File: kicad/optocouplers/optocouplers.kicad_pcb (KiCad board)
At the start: 2 copper layers, 18 parts, among them Q1 PN2222A, U1 ITR9608, U2 ITR9608, U3 ITR9608, U4 ITR9608, U5 ITR9608, U6 ITR9608, U7 ITR9608, U8 ITR9608

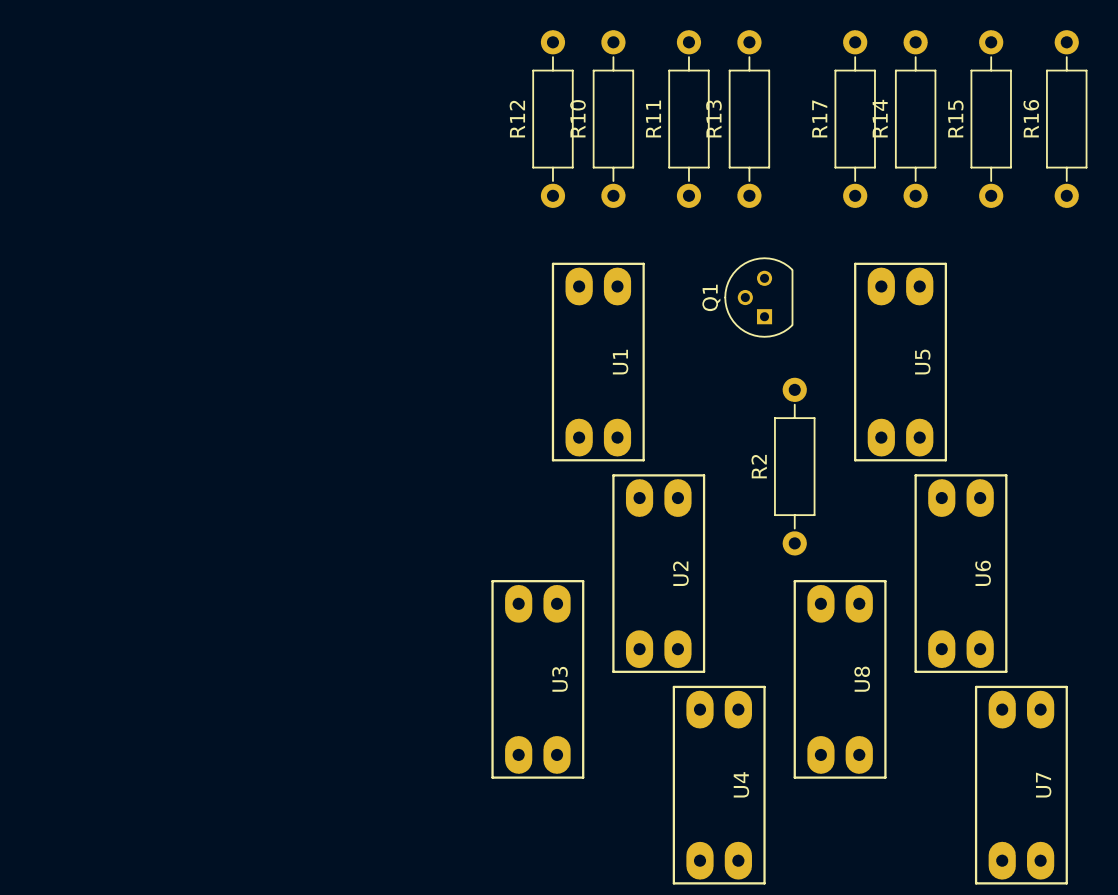
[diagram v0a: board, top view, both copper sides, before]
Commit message: update kicad drawings for optocouplers
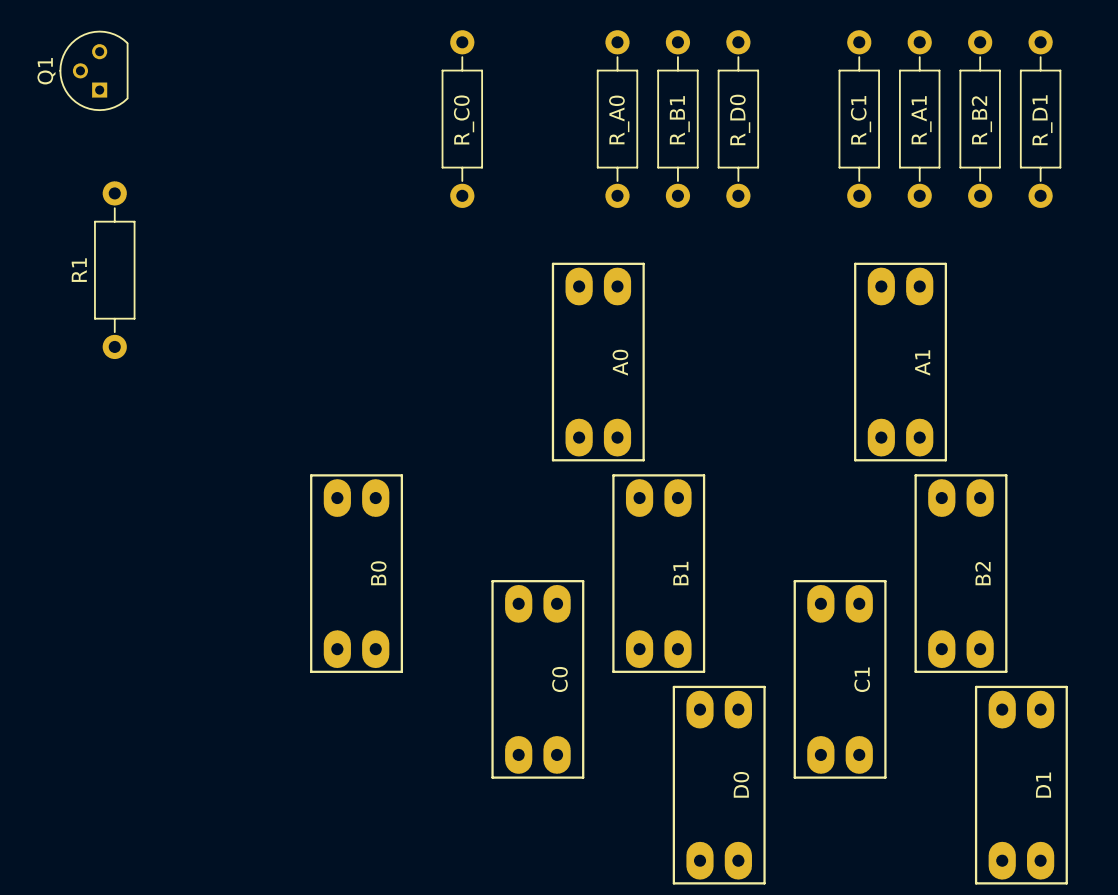
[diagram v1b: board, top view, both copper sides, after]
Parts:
- removed R10, R11, R13, R14, R15, R16, R17: 270R, Resistors_ThroughHole:R_Axial_DIN0207_L6.3mm_D2.5mm_P10.16mm_Horizontal
- added B0: ITR9608, ITR9608:ITR9608, F.Cu at (84.0, 114.0)
- added R_A0: 270R, Resistors_ThroughHole:R_Axial_DIN0207_L6.3mm_D2.5mm_P10.16mm_Horizontal, F.Cu at (101.3, 89.0)
- added R_A1: 270R, Resistors_ThroughHole:R_Axial_DIN0207_L6.3mm_D2.5mm_P10.16mm_Horizontal, F.Cu at (121.3, 89.0)
- added R_B1: 270R, Resistors_ThroughHole:R_Axial_DIN0207_L6.3mm_D2.5mm_P10.16mm_Horizontal, F.Cu at (105.3, 89.0)
- added R_B2: 270R, Resistors_ThroughHole:R_Axial_DIN0207_L6.3mm_D2.5mm_P10.16mm_Horizontal, F.Cu at (125.3, 89.0)
- added R_C1: 270R, Resistors_ThroughHole:R_Axial_DIN0207_L6.3mm_D2.5mm_P10.16mm_Horizontal, F.Cu at (117.3, 89.0)
- added R_D0: 270R, Resistors_ThroughHole:R_Axial_DIN0207_L6.3mm_D2.5mm_P10.16mm_Horizontal, F.Cu at (109.3, 89.0)
- added R_D1: 270R, Resistors_ThroughHole:R_Axial_DIN0207_L6.3mm_D2.5mm_P10.16mm_Horizontal, F.Cu at (129.3, 89.0)
- moved R1 46.8 mm to (68.0, 99.0)
- moved Q1 46.5 mm to (67.0, 82.0)
- moved R_C0 6.00 mm to (91.0, 89.0)
- renumbered U1 to A0, U5 to A1, U2 to B1, U6 to B2, U3 to C0, U8 to C1, U4 to D0, U7 to D1, R2 to R1, R12 to R_C0

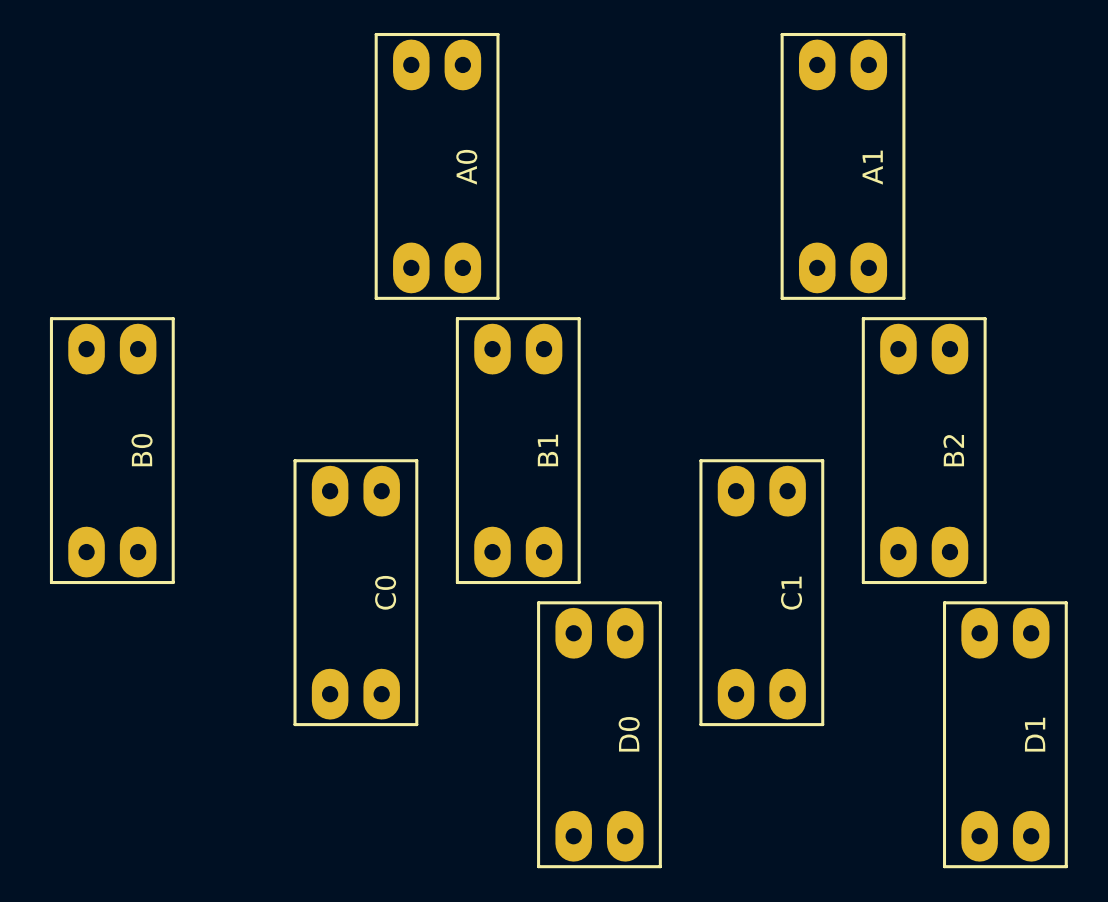
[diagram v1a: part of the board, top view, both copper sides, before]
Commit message: fix reference names on PCB
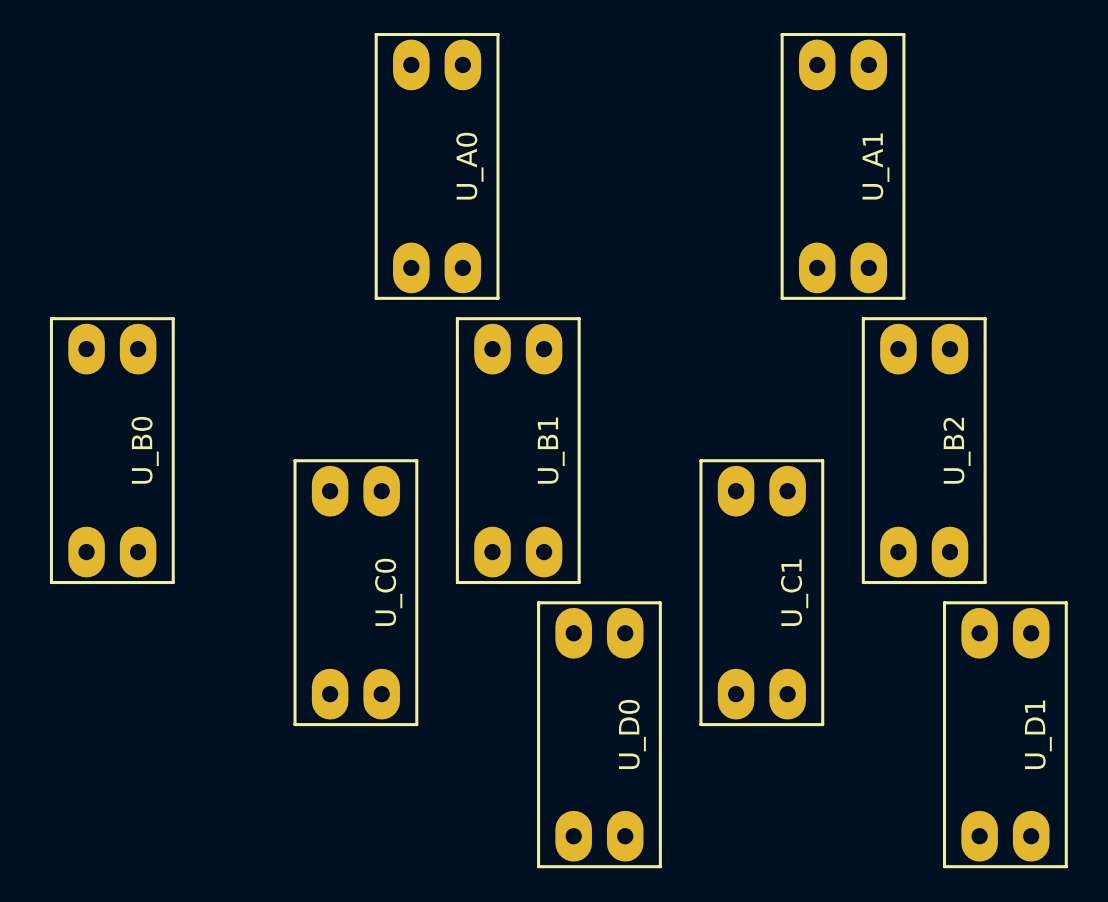
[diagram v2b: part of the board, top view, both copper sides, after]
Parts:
- renumbered A0 to U_A0, A1 to U_A1, B0 to U_B0, B1 to U_B1, B2 to U_B2, C0 to U_C0, C1 to U_C1, D0 to U_D0, D1 to U_D1
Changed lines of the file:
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@@
   (module ITR9608:ITR9608 (layer F.Cu)
     (at 84 114)
-    (fp_text reference B0 (at 1.5 0 90) (layer F.SilkS)
+    (fp_text reference U_B0 (at 1.5 0 90) (layer F.SilkS)
       (effects (font (size 1 1) (thickness 0.15)))
     )
@@
   (module ITR9608:ITR9608 (layer F.Cu)
     (at 100 100)
-    (fp_text reference A0 (at 1.5 0 90) (layer F.SilkS)
+    (fp_text reference U_A0 (at 1.5 0 90) (layer F.SilkS)
       (effects (font (size 1 1) (thickness 0.15)))
     )
@@
   (module ITR9608:ITR9608 (layer F.Cu)
     (at 104 114)
-    (fp_text reference B1 (at 1.5 0 90) (layer F.SilkS)
+    (fp_text reference U_B1 (at 1.5 0 90) (layer F.SilkS)
       (effects (font (size 1 1) (thickness 0.15)))
     )
@@
   (module ITR9608:ITR9608 (layer F.Cu)
     (at 96 121)
-    (fp_text reference C0 (at 1.5 0 90) (layer F.SilkS)
+    (fp_text reference U_C0 (at 1.5 0 90) (layer F.SilkS)
       (effects (font (size 1 1) (thickness 0.15)))
     )
@@
   (module ITR9608:ITR9608 (layer F.Cu)
     (at 108 128)
-    (fp_text reference D0 (at 1.5 0 90) (layer F.SilkS)
+    (fp_text reference U_D0 (at 1.5 0 90) (layer F.SilkS)
       (effects (font (size 1 1) (thickness 0.15)))
     )
@@
   (module ITR9608:ITR9608 (layer F.Cu)
     (at 120 100)
-    (fp_text reference A1 (at 1.5 0 90) (layer F.SilkS)
+    (fp_text reference U_A1 (at 1.5 0 90) (layer F.SilkS)
       (effects (font (size 1 1) (thickness 0.15)))
     )
@@
   (module ITR9608:ITR9608 (layer F.Cu)
     (at 124 114)
-    (fp_text reference B2 (at 1.5 0 90) (layer F.SilkS)
+    (fp_text reference U_B2 (at 1.5 0 90) (layer F.SilkS)
       (effects (font (size 1 1) (thickness 0.15)))
     )
@@
   (module ITR9608:ITR9608 (layer F.Cu)
     (at 128 128)
-    (fp_text reference D1 (at 1.5 0 90) (layer F.SilkS)
+    (fp_text reference U_D1 (at 1.5 0 90) (layer F.SilkS)
       (effects (font (size 1 1) (thickness 0.15)))
     )
@@
   (module ITR9608:ITR9608 (layer F.Cu)
     (at 116 121)
-    (fp_text reference C1 (at 1.5 0 90) (layer F.SilkS)
-      (effects (font (size 1 1) (thickness 0.15)))
-    )
+    (fp_text reference U_C1 (at 1.5 0 90) (layer F.SilkS)
+      (effects (font (size 1 1) (thickness 0.15)))
+    )

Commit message: Update to the latest version of optocoupler pcb design
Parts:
- added J1: Conn_02x13_Top_Bottom, Connectors_Multicomp:Multicomp_MC9A12-2634_2x13x2.54mm_Straight, F.Cu at (51.1, 156.8)
- added Q2: PN2222A, TO_SOT_Packages_THT:TO-92_Molded_Narrow, F.Cu at (303.0, 112.0)
- added Q3: PN2222A, TO_SOT_Packages_THT:TO-92_Molded_Narrow, F.Cu at (97.0, 112.0)
- added Q4: PN2222A, TO_SOT_Packages_THT:TO-92_Molded_Narrow, F.Cu at (307.0, 145.0)
- added Q5: PN2222A, TO_SOT_Packages_THT:TO-92_Molded_Narrow, F.Cu at (88.0, 129.0)
- added Q6: PN2222A, TO_SOT_Packages_THT:TO-92_Molded_Narrow, F.Cu at (305.0, 127.0)
- added Q7: PN2222A, TO_SOT_Packages_THT:TO-92_Molded_Narrow, F.Cu at (77.0, 112.0)
- added Q8: PN2222A, TO_SOT_Packages_THT:TO-92_Molded_Narrow, F.Cu at (311.0, 162.0)
- added U_A10: ITR9608, ITR9608:ITR9608, F.Cu at (277.0, 114.0)
- added U_A11: ITR9608, ITR9608:ITR9608, F.Cu at (286.0, 115.0)
- added U_A2: ITR9608, ITR9608:ITR9608, F.Cu at (136.0, 100.0)
- added U_A3: ITR9608, ITR9608:ITR9608, F.Cu at (215.0, 115.0)
- added U_A4: ITR9608, ITR9608:ITR9608, F.Cu at (224.0, 115.0)
- added U_A5: ITR9608, ITR9608:ITR9608, F.Cu at (233.8, 115.5)
- added U_A6: ITR9608, ITR9608:ITR9608, F.Cu at (243.0, 116.0)
- added U_A7: ITR9608, ITR9608:ITR9608, F.Cu at (252.0, 116.0)
- added U_A8: ITR9608, ITR9608:ITR9608, F.Cu at (261.0, 115.0)
- added U_A9: ITR9608, ITR9608:ITR9608, F.Cu at (268.0, 115.0)
- added U_B10: ITR9608, ITR9608:ITR9608, F.Cu at (277.0, 147.0)
- added U_B11: ITR9608, ITR9608:ITR9608, F.Cu at (286.0, 147.0)
- added U_B12: ITR9608, ITR9608:ITR9608, F.Cu at (295.0, 148.0)
- added U_B3: ITR9608, ITR9608:ITR9608, F.Cu at (143.0, 114.0)
- added U_B4: ITR9608, ITR9608:ITR9608, F.Cu at (226.0, 148.0)
- added U_B5: ITR9608, ITR9608:ITR9608, F.Cu at (234.0, 150.0)
- added U_B6: ITR9608, ITR9608:ITR9608, F.Cu at (244.0, 150.0)
- added U_B7: ITR9608, ITR9608:ITR9608, F.Cu at (251.0, 151.0)
- added U_B8: ITR9608, ITR9608:ITR9608, F.Cu at (260.0, 149.0)
- added U_B9: ITR9608, ITR9608:ITR9608, F.Cu at (268.0, 148.0)
- added U_C10: ITR9608, ITR9608:ITR9608, F.Cu at (277.2, 131.0)
- added U_C11: ITR9608, ITR9608:ITR9608, F.Cu at (286.0, 132.0)
- added U_C2: ITR9608, ITR9608:ITR9608, F.Cu at (136.0, 121.0)
- added U_C3: ITR9608, ITR9608:ITR9608, F.Cu at (153.0, 121.0)
- added U_C4: ITR9608, ITR9608:ITR9608, F.Cu at (225.0, 132.0)
- added U_C5: ITR9608, ITR9608:ITR9608, F.Cu at (234.0, 133.0)
- added U_C6: ITR9608, ITR9608:ITR9608, F.Cu at (243.0, 133.0)
- added U_C7: ITR9608, ITR9608:ITR9608, F.Cu at (252.0, 133.0)
- added U_C8: ITR9608, ITR9608:ITR9608, F.Cu at (261.0, 133.0)
- added U_C9: ITR9608, ITR9608:ITR9608, F.Cu at (270.7, 131.0)
- added U_D10: ITR9608, ITR9608:ITR9608, F.Cu at (278.0, 172.0)
- added U_D2: ITR9608, ITR9608:ITR9608, F.Cu at (143.0, 128.0)
- added U_D3: ITR9608, ITR9608:ITR9608, F.Cu at (160.0, 128.0)
- added U_D4: ITR9608, ITR9608:ITR9608, F.Cu at (225.0, 167.0)
- added U_D5: ITR9608, ITR9608:ITR9608, F.Cu at (235.0, 170.0)
- added U_D6: ITR9608, ITR9608:ITR9608, F.Cu at (244.0, 169.0)
- added U_D7: ITR9608, ITR9608:ITR9608, F.Cu at (252.0, 169.0)
- added U_D8: ITR9608, ITR9608:ITR9608, F.Cu at (261.0, 170.0)
- added U_D9: ITR9608, ITR9608:ITR9608, F.Cu at (269.0, 171.0)
- moved Q1 30.5 mm to (93.0, 98.0)
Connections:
- R1 pad 1: (no net) -> arduino_D5
- R_A0 pad 1: Net-(R12-Pad1) -> Net-(R_A0-Pad1)
- R_A1 pad 1: Net-(R12-Pad1) -> Net-(R_A1-Pad1)
- R_B1 pad 1: Net-(R12-Pad1) -> Net-(R_B1-Pad1)
- R_B2 pad 1: Net-(R12-Pad1) -> Net-(R_B2-Pad1)
- R_C0 pad 1: Net-(R12-Pad1) -> Net-(R_C0-Pad1)
- R_C1 pad 1: Net-(R12-Pad1) -> Net-(R_C1-Pad1)
- R_D0 pad 1: Net-(R12-Pad1) -> Net-(R_D0-Pad1)
- R_D1 pad 1: Net-(R12-Pad1) -> Net-(R_D1-Pad1)
- U_A0 pad 1: Net-(R10-Pad1) -> Net-(R_A0-Pad1)
- U_A0 pad 3: (no net) -> arduino_A0
- U_A1 pad 1: Net-(R14-Pad1) -> Net-(R_A1-Pad1)
- U_A1 pad 3: (no net) -> arduino_A1
- U_B0 pad 1: Net-(R11-Pad1) -> Net-(R_B0-Pad1)
- U_B0 pad 2: Net-(Q1-Pad3) -> Net-(Q7-Pad3)
- U_B0 pad 3: (no net) -> arduino_A0
- U_B1 pad 1: Net-(R11-Pad1) -> Net-(R_B1-Pad1)
- U_B1 pad 2: Net-(Q1-Pad3) -> Net-(Q3-Pad3)
- U_B1 pad 3: (no net) -> arduino_A0
- U_B2 pad 1: Net-(R15-Pad1) -> Net-(R_B2-Pad1)
- U_B2 pad 2: Net-(Q1-Pad3) -> Net-(Q3-Pad3)
- U_B2 pad 3: (no net) -> arduino_A1
- U_C0 pad 1: Net-(R12-Pad1) -> Net-(R_C0-Pad1)
- U_C0 pad 2: Net-(Q1-Pad3) -> Net-(Q5-Pad3)
- U_C0 pad 3: (no net) -> arduino_A0
- U_C1 pad 1: Net-(R17-Pad1) -> Net-(R_C1-Pad1)
- U_C1 pad 2: Net-(Q1-Pad3) -> Net-(Q5-Pad3)
- U_C1 pad 3: (no net) -> arduino_A1
- U_D0 pad 1: Net-(R13-Pad1) -> Net-(R_D0-Pad1)
- U_D0 pad 2: Net-(Q1-Pad3) -> Net-(Q7-Pad3)
- U_D0 pad 3: (no net) -> arduino_A1
- U_D1 pad 1: Net-(R16-Pad1) -> Net-(R_D1-Pad1)
- U_D1 pad 2: Net-(Q1-Pad3) -> Net-(Q7-Pad3)
- U_D1 pad 3: (no net) -> arduino_A2
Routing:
- net Net-(Q7-Pad3): track 0.00 -> 50.5 mm
- net Net-(Q5-Pad3): track 0.00 -> 46.0 mm
- net arduino_A1: track 0.00 -> 39.6 mm
- net Net-(R_D1-Pad1): track 0.00 -> 34.0 mm
- net Net-(R_D0-Pad1): track 0.00 -> 34.0 mm
- net Net-(Q1-Pad3): track 0.00 -> 30.2 mm
- net Net-(Q3-Pad3): track 0.00 -> 29.0 mm
- net arduino_A0: track 0.00 -> 28.4 mm
- net Net-(R_C1-Pad1): track 0.00 -> 28.1 mm
- net Net-(R_B2-Pad1): track 0.00 -> 20.0 mm
- net Net-(R_B1-Pad1): track 0.00 -> 20.0 mm
- net Net-(R_A1-Pad1): track 0.00 -> 6.00 mm
- net Net-(R_A0-Pad1): track 0.00 -> 6.00 mm
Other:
- net class Default: clearance 0.2 -> 0.6; trace_width 0.25 -> 0.6
- rule trace_clearance: 0.2 -> 0.6
- rule trace_min: 0.2 -> 0.3
